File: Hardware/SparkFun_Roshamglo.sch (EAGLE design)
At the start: 35 parts, among them IC1 ATTINY84A, J1 ICSP, J2 USBPCB, Q1 500mA/300V, U1 IR-Receiver, U3 AP2112K-3.3V

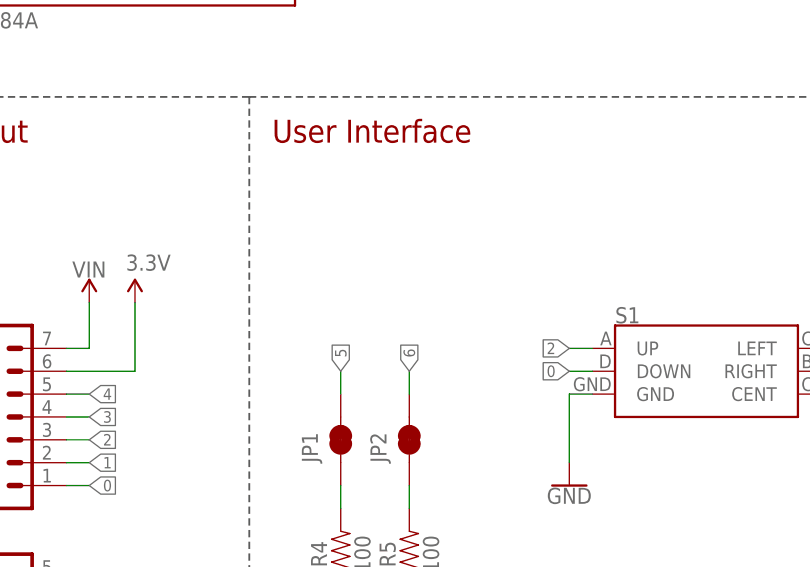
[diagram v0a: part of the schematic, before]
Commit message: V01 changes
- Fixed version number DRC error
- Added pin 1 marker to Attiny84 to make orientation obvious after
placement.
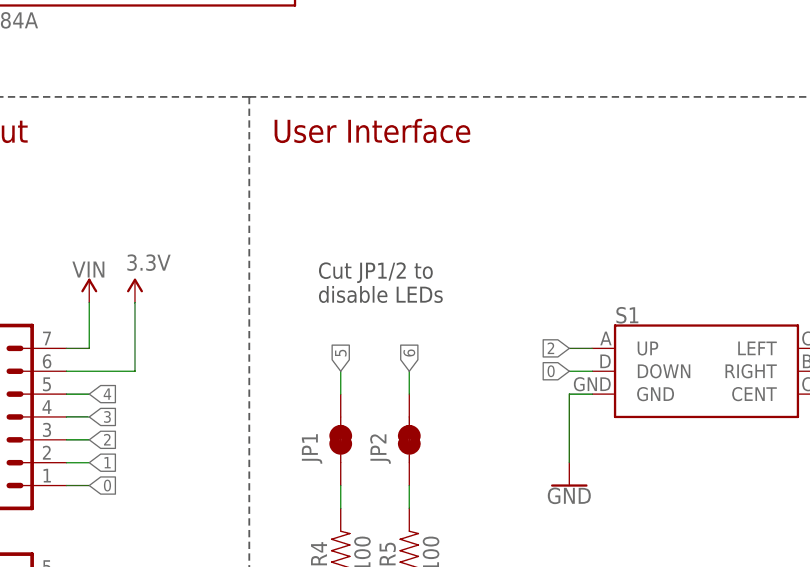
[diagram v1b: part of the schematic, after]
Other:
- note added: "Cut JP1/2 to disable LEDs"
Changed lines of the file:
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@@
 <text x="129.54" y="116.84" size="2.54" layer="94">IO Breakout</text>
 <wire x1="127" y1="121.92" x2="127" y2="35.56" width="0.2032" layer="97" style="shortdash"/>
+<text x="180.34" y="99.06" size="1.778" layer="97">Cut JP1/2 to
+disable LEDs</text>
 </plain>
 <instances>

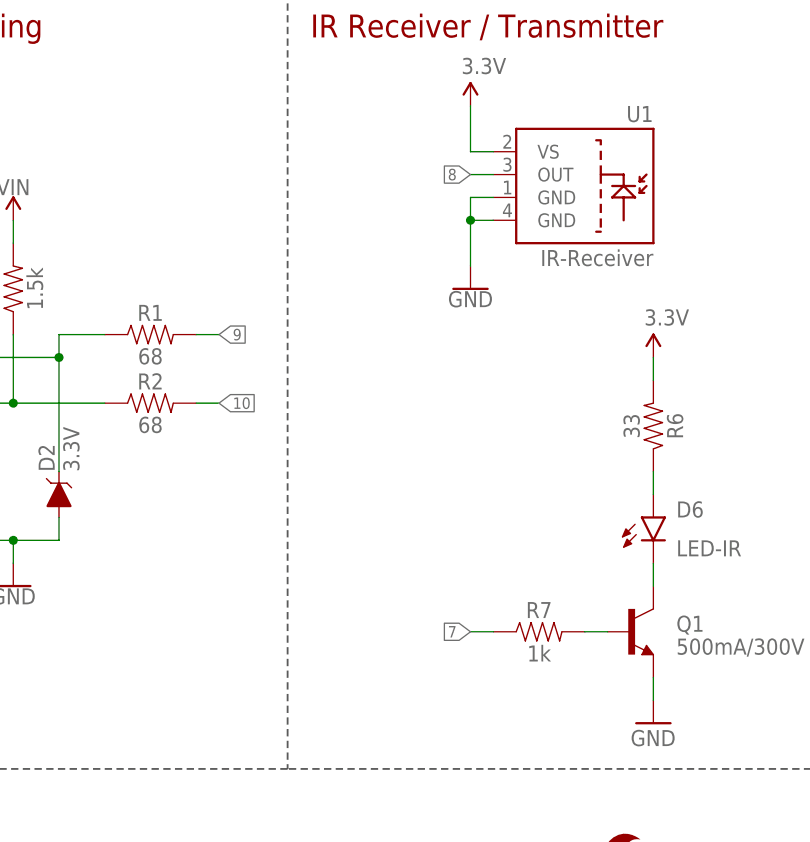
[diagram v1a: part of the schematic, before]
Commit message: v01 changes
- Extended USB connector length 0.1"
- Added jumpers to pins 7 and 8
- Changed project name silk to single word
- Added PWM pin labels
- Rotated pin names 90 deg
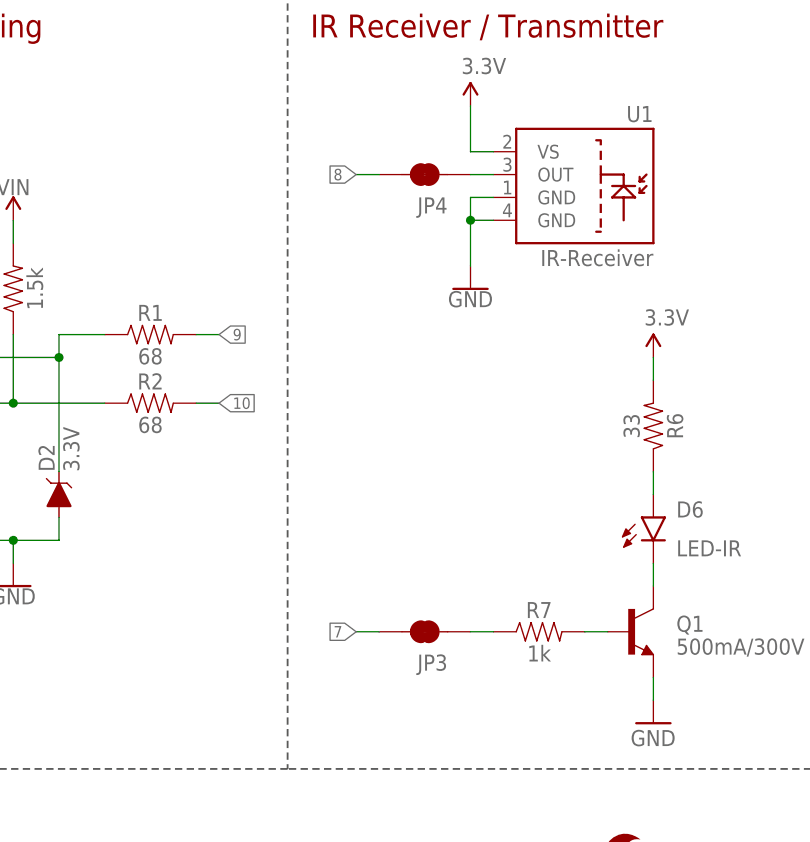
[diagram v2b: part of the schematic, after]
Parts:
- added JP3, JP4: JUMPER-SMT_2_NC_TRACE_SILK, SparkFun-Jumpers:JUMPER-SMT_2_NC_TRACE_SILK
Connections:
- new net N$10: JP3.1, R7.1
- new net N$9: JP4.1, U1.OUT
- net 7: now also JP3.2; no longer R7.1
- net 8: now also JP4.2; no longer U1.OUT
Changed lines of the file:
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@@
 <part name="SUPPLY8" library="SparkFun-PowerSymbols" deviceset="VIN" device=""/>
 <part name="SUPPLY10" library="SparkFun-Aesthetics" deviceset="3.3V" device=""/>
+<part name="JP3" library="SparkFun-Jumpers" deviceset="JUMPER-SMT_2_NC_TRACE" device="_SILK" value=""/>
+<part name="JP4" library="SparkFun-Jumpers" deviceset="JUMPER-SMT_2_NC_TRACE" device="_SILK" value=""/>
 </parts>
 <sheets>
@@
 <instance part="SUPPLY8" gate="G$1" x="154.94" y="99.06"/>
 <instance part="SUPPLY10" gate="G$1" x="160.02" y="99.06"/>
+<instance part="JP3" gate="G$1" x="73.66" y="50.8" rot="R180"/>
+<instance part="JP4" gate="G$1" x="73.66" y="101.6" rot="R180"/>
 </instances>
 <busses>
@@
 </segment>
 <segment>
-<pinref part="U1" gate="G$1" pin="OUT"/>
-<wire x1="81.28" y1="101.6" x2="78.74" y2="101.6" width="0.1524" layer="91"/>
-<label x="78.74" y="101.6" size="1.27" layer="95" rot="R180" xref="yes"/>
-</segment>
-<segment>
 <pinref part="J5" gate="G$1" pin="5"/>
 <wire x1="152.4" y1="68.58" x2="154.94" y2="68.58" width="0.1524" layer="91"/>
 <label x="154.94" y="68.58" size="1.27" layer="95" xref="yes"/>
 </segment>
+<segment>
+<pinref part="JP4" gate="G$1" pin="2"/>
+<wire x1="68.58" y1="101.6" x2="66.04" y2="101.6" width="0.1524" layer="91"/>
+<label x="66.04" y="101.6" size="1.27" layer="95" rot="R180" xref="yes"/>
+</segment>
 </net>
 <net name="9" class="0">
@@
 </segment>
 <segment>
-<pinref part="R7" gate="G$1" pin="1"/>
-<wire x1="81.28" y1="50.8" x2="78.74" y2="50.8" width="0.1524" layer="91"/>
-<label x="78.74" y="50.8" size="1.27" layer="95" rot="R180" xref="yes"/>
-</segment>
-<segment>
 <pinref part="J5" gate="G$1" pin="4"/>
 <wire x1="152.4" y1="66.04" x2="154.94" y2="66.04" width="0.1524" layer="91"/>
 <label x="154.94" y="66.04" size="1.27" layer="95" xref="yes"/>
+</segment>
+<segment>
+<pinref part="JP3" gate="G$1" pin="2"/>
+<wire x1="68.58" y1="50.8" x2="66.04" y2="50.8" width="0.1524" layer="91"/>
+<label x="66.04" y="50.8" size="1.27" layer="95" rot="R180" xref="yes"/>
 </segment>
 </net>
@@
 </segment>
 </net>
+<net name="N$9" class="0">
+<segment>
+<pinref part="JP4" gate="G$1" pin="1"/>
+<pinref part="U1" gate="G$1" pin="OUT"/>
+<wire x1="78.74" y1="101.6" x2="81.28" y2="101.6" width="0.1524" layer="91"/>
+</segment>
+</net>
+<net name="N$10" class="0">
+<segment>
+<pinref part="JP3" gate="G$1" pin="1"/>
+<pinref part="R7" gate="G$1" pin="1"/>
+<wire x1="78.74" y1="50.8" x2="81.28" y2="50.8" width="0.1524" layer="91"/>
+</segment>
+</net>

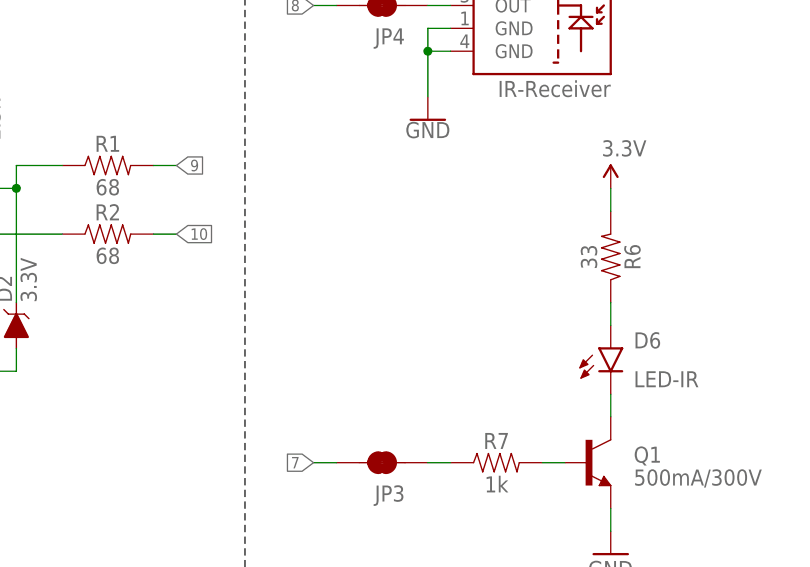
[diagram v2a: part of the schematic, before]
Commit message: v01 changes
- Added labels to jumpers
- Cleaned up a couple traces
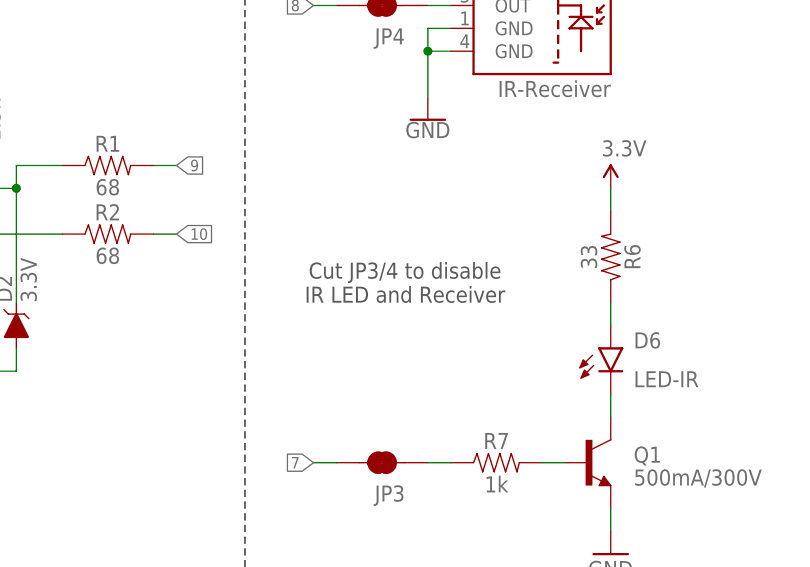
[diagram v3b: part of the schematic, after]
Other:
- note added: "Cut JP3/4 to disable IR LED and Receiver"
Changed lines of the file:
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@@
 <text x="180.34" y="99.06" size="1.778" layer="97">Cut JP1/2 to
 disable LEDs</text>
+<text x="76.2" y="68.58" size="1.778" layer="97" align="bottom-center">Cut JP3/4 to disable
+IR LED and Receiver</text>
 </plain>
 <instances>

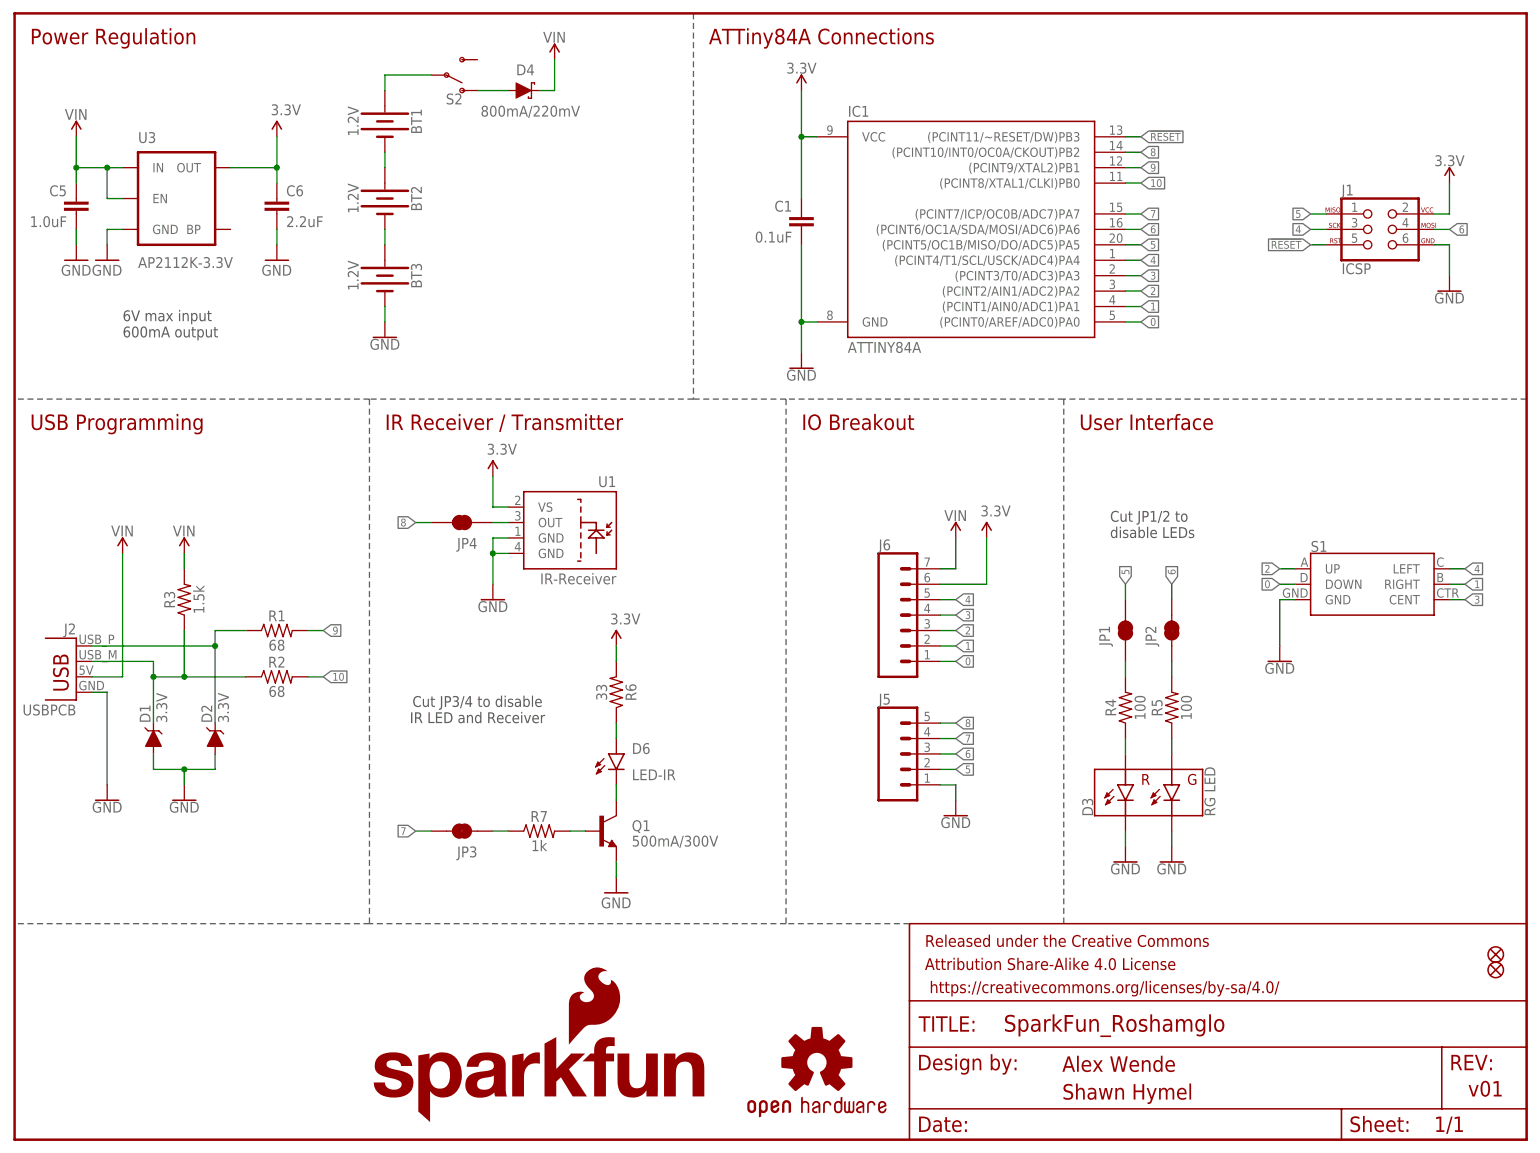
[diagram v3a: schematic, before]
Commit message: Design Review Changes
- removed ISP
- added 10k to reset pin
- broke out reset pin
- Moved components away from SS pins
- Changed route out to dimmention layer
- moved lanyard hole away from edge of board
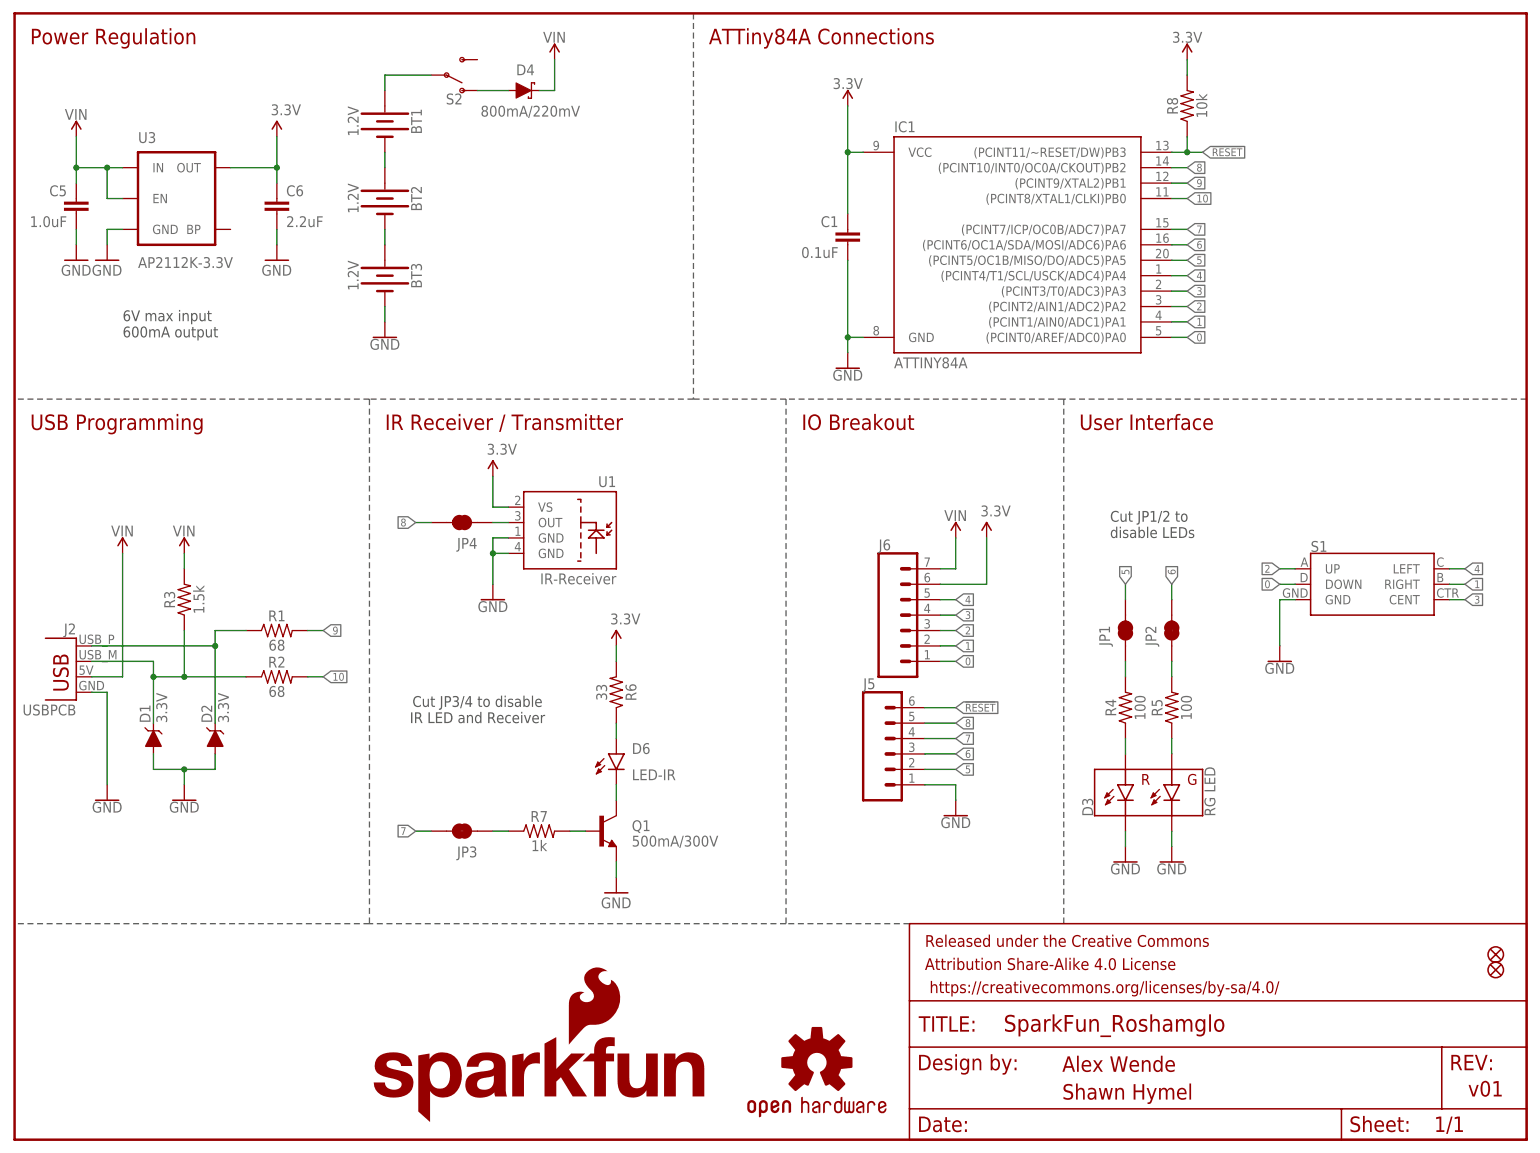
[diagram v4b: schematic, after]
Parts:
- removed J1: ICSP, SparkFun-Connectors:AVR_SPI_PROG_3X2PTH
- added R8: 10k, SparkFun-Resistors:10KOHM-0603-1/10W-1%
- J5: device SparkFun-Connectors:CONN_05NO_SILK -> SparkFun-Connectors:CONN_06NO_SILK_FEMALE_PTH
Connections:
- net !RESET: now also J5.6, R8.1; no longer J1.5
- net 3.3V: now also R8.2; no longer J1.2
- net 4: no longer J1.3
- net 5: no longer J1.1
- net 6: no longer J1.4
- net GND: no longer J1.6
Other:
- moved on the sheet: C1, IC1

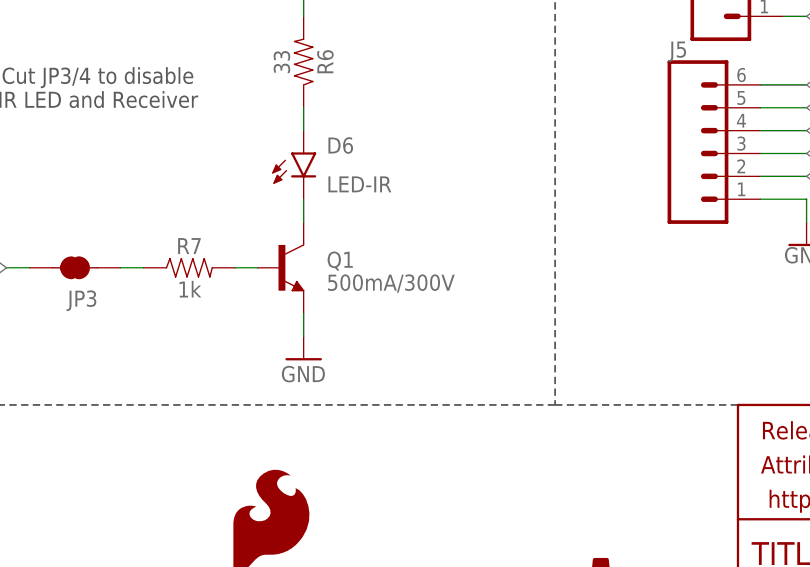
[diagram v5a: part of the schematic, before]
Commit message: Replaced transistor
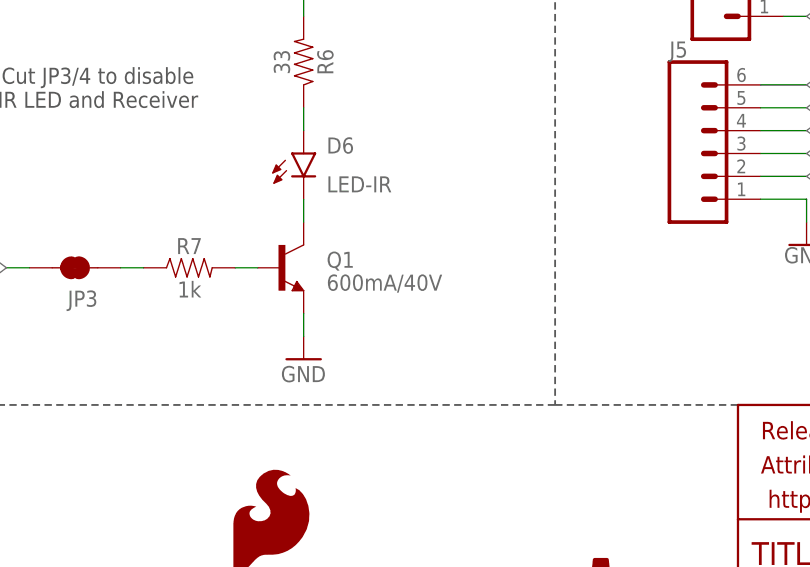
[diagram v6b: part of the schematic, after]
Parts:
- Q1: value 500mA/300V -> 600mA/40V; device SparkFun-DiscreteSemi:TRANS_NPN-MMBTA42 -> SparkFun-DiscreteSemi:TRANS_NPN-MMBT2222AL
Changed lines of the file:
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@@
 <part name="JP1" library="SparkFun-Jumpers" deviceset="JUMPER-SMT_2_NC_TRACE" device="_SILK" value=""/>
 <part name="JP2" library="SparkFun-Jumpers" deviceset="JUMPER-SMT_2_NC_TRACE" device="_SILK" value=""/>
-<part name="Q1" library="SparkFun-DiscreteSemi" deviceset="TRANS_NPN" device="-MMBTA42" value="500mA/300V"/>
+<part name="Q1" library="SparkFun-DiscreteSemi" deviceset="TRANS_NPN" device="-MMBT2222AL" value="600mA/40V"/>
 <part name="R7" library="SparkFun-Resistors" deviceset="1KOHM" device="-0603-1/10W-1%" value="1k"/>
 <part name="GND11" library="SparkFun-Aesthetics" deviceset="GND" device=""/>

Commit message: v02 Changes
- Moved IR LED to GPIO 5
- Moved red and green LEDs to GPIO 7 and 8
- Moved IR receiver to GPIO 3
- Moved center switch to GPIO 6
- Increased distance between batteries
- Increased board size to 1.4"
- Added reset switch
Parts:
- added S3: MOMENTARY-SWITCH-SPST-SMD-4.6X2.8MM, SparkFun-Switches:MOMENTARY-SWITCH-SPST-SMD-4.6X2.8MM
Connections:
- net !RESET: now also S3.1
- net 3: now also JP4.2; no longer S1.CENT
- net 5: now also JP3.2; no longer JP1.2
- net 6: now also S1.CENT; no longer JP2.2
- net 7: now also JP2.2; no longer JP3.2
- net 8: now also JP1.2; no longer JP4.2
- net GND: now also S3.2
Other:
- note added: "v02"
- note removed: "v01"
